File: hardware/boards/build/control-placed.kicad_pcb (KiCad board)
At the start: 4 copper layers, 177.9 x 107.5 mm, 132 parts

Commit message: Fix firmware
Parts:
- removed the REF** at (69.8, 51.4)
- removed the REF** at (69.8, 36.2)
- removed the REF** at (39.4, 59.0)
- removed the REF** at (77.4, 21.0)
- removed the REF** at (54.6, 43.8)
- removed the REF** at (69.8, 21.0)
- removed the REF** at (25.9, 71.9)
- removed the REF** at (54.6, 36.2)
- removed the REF** at (54.6, 59.0)
- added REF**: R_Array_Convex_4x0603, ResArray4x0603:R_Array_Convex_4x0603, B.Cu at (31.8, 59.0)
- added REF**: SOIC-16, 74HC165D:SOIC-16, B.Cu at (77.4, 51.4)
- added REF**: SOIC-16, 74HC165D:SOIC-16, B.Cu at (62.2, 59.0)
- added REF**: R_Array_Convex_4x0603, ResArray4x0603:R_Array_Convex_4x0603, B.Cu at (77.4, 36.2)
- added REF**: R_Array_Convex_4x0603, ResArray4x0603:R_Array_Convex_4x0603, B.Cu at (77.4, 28.6)
- added REF**: SOIC-16, 74HC165D:SOIC-16, B.Cu at (47.0, 59.0)
- added REF**: R_Array_Convex_4x0603, ResArray4x0603:R_Array_Convex_4x0603, B.Cu at (69.8, 28.6)
- added REF**: SOIC-16, 74HC165D:SOIC-16, B.Cu at (62.2, 43.8)
- added REF**: R_Array_Convex_4x0603, ResArray4x0603:R_Array_Convex_4x0603, B.Cu at (62.2, 28.6)
- moved C10 92.3 mm to (85.0, 5.80)
- moved C18 87.1 mm to (115.2, 63.9)
- moved C15 85.2 mm to (85.0, 21.0)
- moved R16 83.9 mm to (39.4, 28.6)
- moved C16 80.6 mm to (47.0, 21.0)
- moved C8 75.8 mm to (107.9, 95.2)
- moved C20 53.7 mm to (39.4, 43.8)
- moved C4 53.7 mm to (31.8, 43.8)
- moved C21 51.0 mm to (77.4, 5.80)
- moved C22 51.0 mm to (77.4, 13.4)
- moved C5 34.0 mm to (31.8, 51.4)
- moved C17 34.0 mm to (69.8, 13.4)
- moved C12 32.3 mm to (122.6, 17.7)
- moved C25 31.3 mm to (115.7, 71.7)
- moved R1 31.2 mm to (25.9, 71.9)
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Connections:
- REF** pad 1: buttons-1-3 -> buttons-1-4
- REF** pad 2: buttons-R2A-3 -> buttons-R2A-5
- REF** pad 3: buttons-R3A-3 -> buttons-R3A-5
- REF** pad 4: buttons-R4A-4 -> buttons-R4A-6
- REF** pad 10: QH -> lv
- REF** pad 11: buttons-1-5 -> buttons-1-2
- REF** pad 12: buttons-R2A-2 -> buttons-R2A-4
- REF** pad 13: buttons-R3A-2 -> buttons-R3A-4
- REF** pad 14: buttons-R4A-3 -> buttons-R4A-5
- REF** pad 3: buttons-1-3 -> buttons-1-4
- REF** pad 4: buttons-R2A-3 -> buttons-R2A-5
- REF** pad 5: buttons-R3A-3 -> buttons-R3A-5
- REF** pad 6: buttons-R4A-4 -> buttons-R4A-6
- REF** pad 7: buttons.sr2-QH_N -> QH_N
- REF** pad 9: buttons-QH -> QH
- REF** pad 1: buttons-1 -> buttons-1-7
- REF** pad 2: buttons-R2A -> buttons-R2A-7
- REF** pad 3: buttons-R3A-1 -> R3A
- REF** pad 4: buttons-R4A -> buttons-R4A-2
- REF** pad 1: buttons-1-2 -> buttons-1-6
- REF** pad 2: buttons-R2A-4 -> buttons-R2A-6
- REF** pad 3: buttons-R3A-4 -> buttons-R3A-6
- REF** pad 4: buttons-R4A-5 -> buttons-R4A-7
- REF** pad 1: buttons-1-4 -> buttons-1-3
- REF** pad 2: buttons-R2A-5 -> buttons-R2A-3
- REF** pad 3: buttons-R3A-5 -> buttons-R3A-3
- REF** pad 4: buttons-R4A-6 -> buttons-R4A-4

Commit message: Fix visuals
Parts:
- removed the REF** at (107.9, 63.9)
- removed the REF** at (85.0, 36.2)
- added REF**: R_Array_Convex_4x0603, ResArray4x0603:R_Array_Convex_4x0603, B.Cu at (92.6, 59.0)
- added REF**: R_Array_Convex_4x0603, ResArray4x0603:R_Array_Convex_4x0603, B.Cu at (92.6, 51.4)
- moved C9 124.6 mm to (21.4, 13.4)
- moved C18 116.9 mm to (13.8, 5.79)
- moved R7 98.7 mm to (158.0, 6.00)
- moved C25 89.9 mm to (54.6, 5.80)
- moved R6 88.5 mm to (150.0, 6.00)
- moved C14 87.7 mm to (6.47, 52.5)
- moved C23 81.6 mm to (6.47, 61.4)
- moved R9 81.1 mm to (31.8, 43.8)
- moved R8 72.5 mm to (122.6, 8.58)
- moved C13 64.9 mm to (31.8, 36.2)
- moved REF** 62.3 mm to (122.6, 17.7)
- moved R16 54.0 mm to (88.4, 51.2)
- moved C10 53.7 mm to (31.8, 13.4)
- moved C7 53.7 mm to (39.4, 13.4)
- moved C6 53.2 mm to (39.4, 21.0)
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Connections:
- REF** pad 1: buttons-1 -> buttons-1-7
- REF** pad 2: buttons-R2A -> buttons-R2A-7
- REF** pad 3: buttons-R3A-1 -> R3A
- REF** pad 4: buttons-R4A -> buttons-R4A-2
- REF** pad 7: QH_N -> (no net)
- REF** pad 7: buttons.sr5-QH_N -> (no net)
- REF** pad 3: NC -> (no net)
- REF** pad 1: buttons-1-5 -> buttons-1-1
- REF** pad 2: buttons-R2A-2 -> R2A
- REF** pad 3: buttons-R3A-2 -> buttons-R3A
- REF** pad 4: buttons-R4A-3 -> R4A
- REF** pad 7: buttons.sr4-QH_N -> (no net)
- REF** pad 7: buttons.sr2-QH_N -> (no net)
- REF** pad 1: buttons-1-3 -> buttons-1-4
- REF** pad 2: buttons-R2A-3 -> buttons-R2A-5
- REF** pad 3: buttons-R3A-3 -> buttons-R3A-5
- REF** pad 4: buttons-R4A-4 -> buttons-R4A-6
- REF** pad 1: buttons-1-2 -> buttons-1-5
- REF** pad 2: buttons-R2A-4 -> buttons-R2A-2
- REF** pad 3: buttons-R3A-4 -> buttons-R3A-2
- REF** pad 4: buttons-R4A-5 -> buttons-R4A-3
- REF** pad 1: buttons-1-1 -> buttons-1-3
- REF** pad 2: R2A -> buttons-R2A-3
- REF** pad 3: buttons-R3A -> buttons-R3A-3
- REF** pad 4: R4A -> buttons-R4A-4
- REF** pad 7: buttons.sr3-QH_N -> (no net)
- U6 pad 21: INTB -> (no net)
- U7 pad 21: leds.led_b-INTB -> (no net)
- U8 pad 21: leds.led_c-INTB -> (no net)

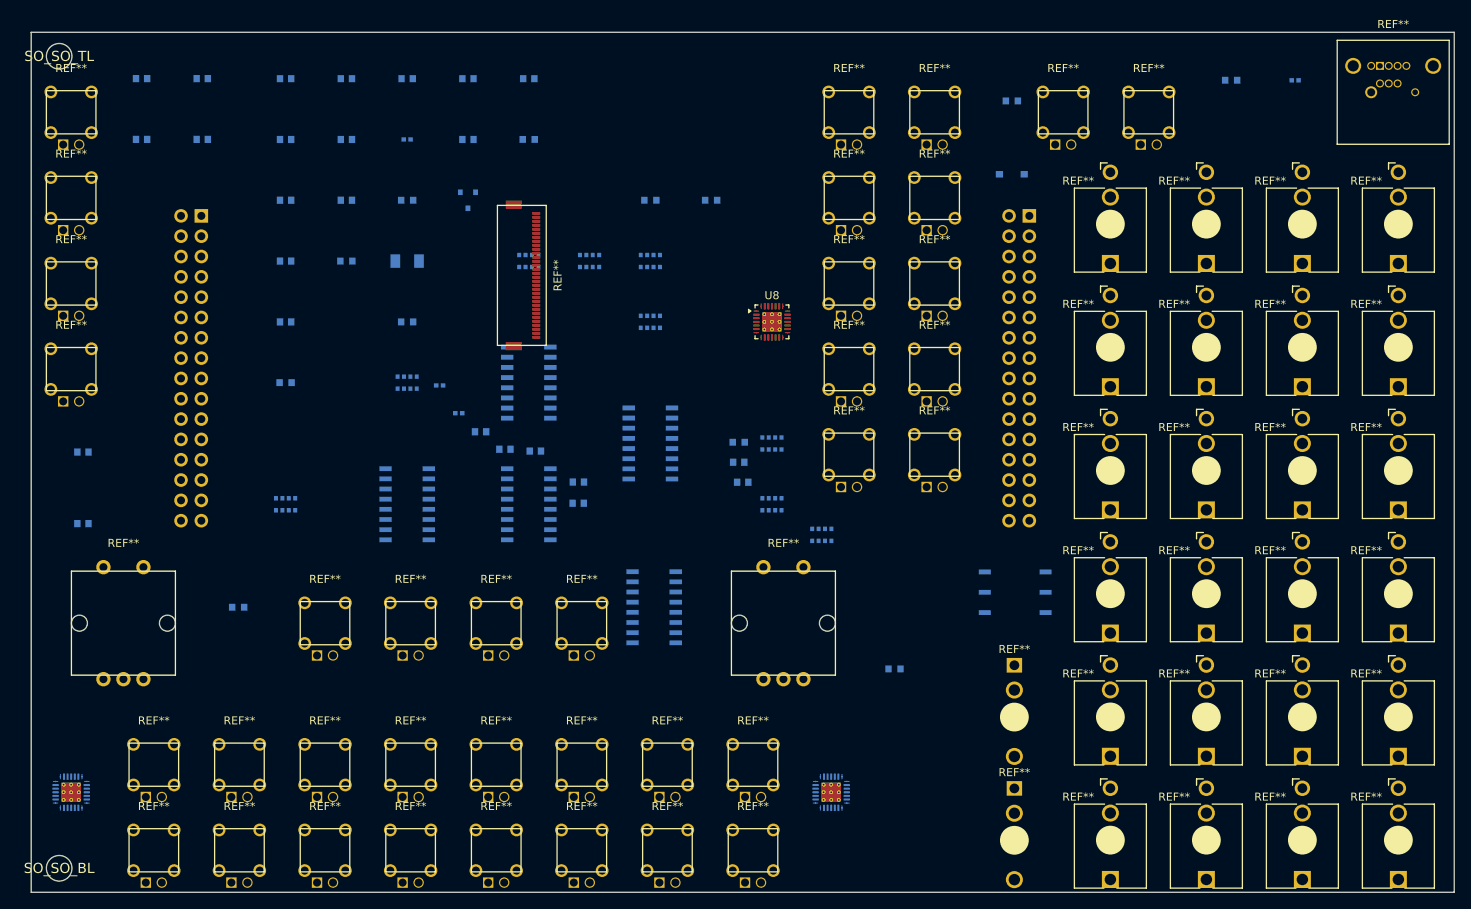
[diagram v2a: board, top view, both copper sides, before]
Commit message: production check command and fixes coming out of that
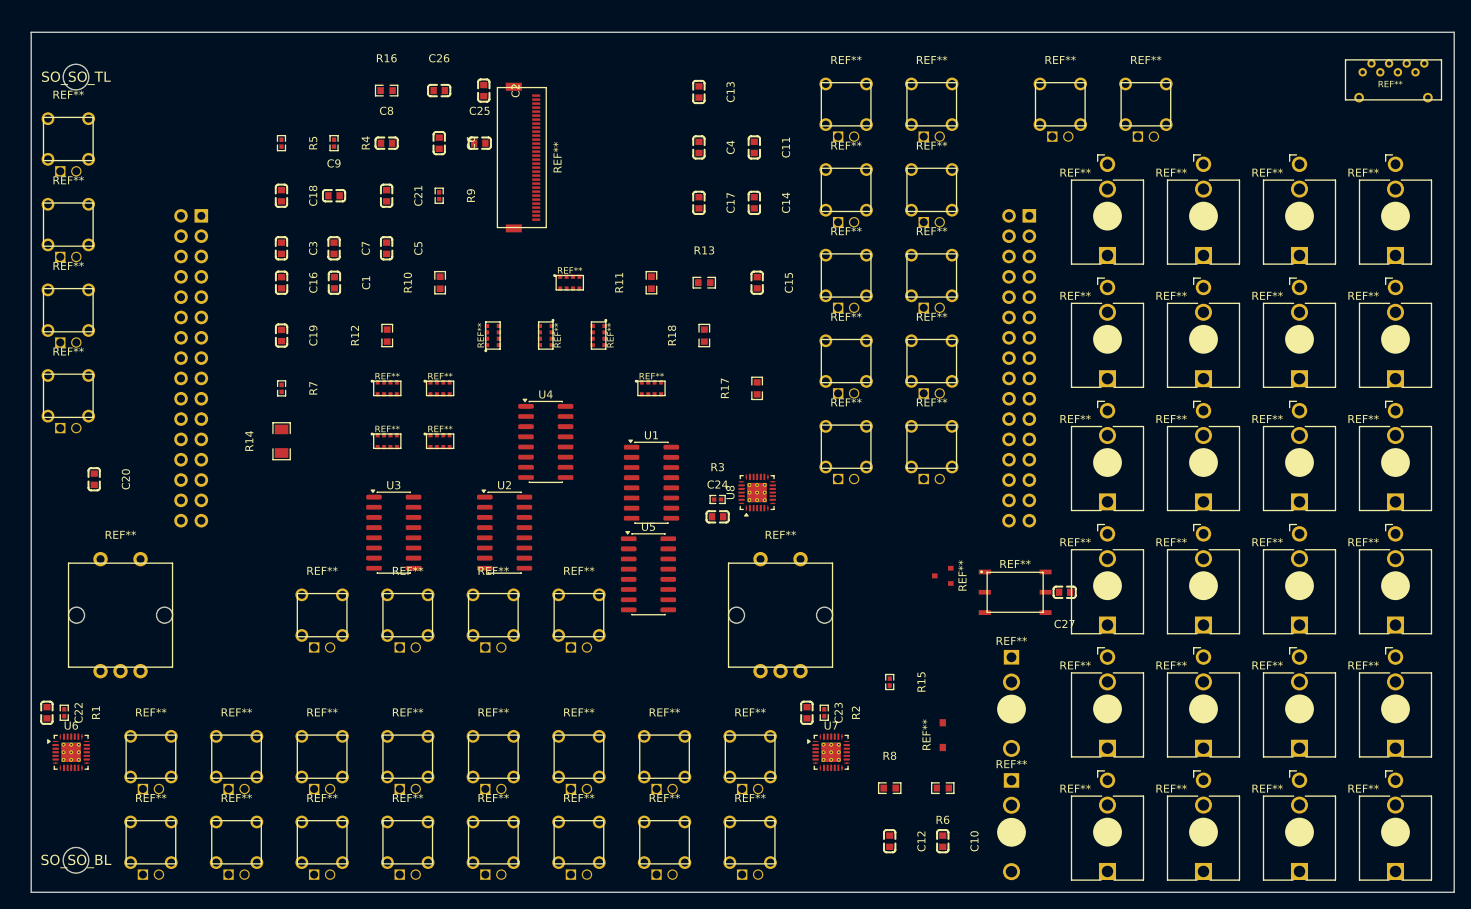
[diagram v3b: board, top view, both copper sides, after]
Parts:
- removed the REF** at (68.8, 102.2)
- removed the REF** at (134.9, 79.1)
- removed the REF** at (94.0, 73.9)
- removed the REF** at (79.5, 91.5)
- removed the REF** at (134.9, 17.5)
- removed the REF** at (58.1, 73.9)
- removed the REF** at (146.9, 48.3)
- removed the REF** at (5.00, 42.1)
- removed the REF** at (112.9, 10.0)
- removed the REF** at (112.9, 31.4)
- removed the REF** at (122.9, 101.0)
- removed the REF** at (146.9, 79.1)
- removed the REF** at (36.7, 73.9)
- removed the REF** at (146.9, 32.9)
- removed the REF** at (134.9, 63.7)
- removed the REF** at (134.9, 48.3)
- removed the REF** at (36.7, 102.2)
- removed the REF** at (146.9, 94.5)
- removed the REF** at (170.9, 94.5)
- removed the REF** at (112.9, 52.8)
- removed the REF** at (5.00, 10.0)
- removed the REF** at (102.2, 52.8)
- removed the REF** at (47.4, 91.5)
- removed the REF** at (134.9, 94.5)
- removed the REF** at (170.9, 48.3)
- removed the REF** at (79.5, 102.2)
- removed the REF** at (68.8, 73.9)
- removed the REF** at (122.9, 85.6)
- removed the REF** at (15.3, 102.2)
- removed the REF** at (158.9, 79.1)
- removed the REF** at (129.0, 10.0)
- removed the REF** at (170.9, 17.5)
- removed the REF** at (90.2, 102.2)
- removed the REF** at (102.2, 20.7)
- removed the REF** at (112.9, 42.1)
- removed the REF** at (58.1, 102.2)
- removed the REF** at (11.5, 73.9)
- removed the REF** at (158.9, 63.7)
- removed the REF** at (5.00, 31.4)
- removed the REF** at (146.9, 17.5)
- removed the REF** at (26.0, 102.2)
- removed the REF** at (112.9, 20.7)
- removed the REF** at (170.9, 79.1)
- removed the REF** at (158.9, 94.5)
- removed the REF** at (90.2, 91.5)
- removed the REF** at (5.00, 20.7)
- removed the REF** at (158.9, 32.9)
- removed the REF** at (58.1, 91.5)
- removed the REF** at (170.9, 32.9)
- removed the REF** at (146.9, 63.7)
- removed the REF** at (134.9, 32.9)
- removed the REF** at (68.8, 91.5)
- removed the REF** at (170.9, 63.7)
- removed the REF** at (26.0, 91.5)
- removed the REF** at (139.7, 10.0)
- removed the REF** at (102.2, 10.0)
- removed the REF** at (158.9, 17.5)
- removed the REF** at (102.2, 42.1)
- removed the REF** at (47.4, 102.2)
- removed the REF** at (36.7, 91.5)
- removed the REF** at (102.2, 31.4)
- removed the REF** at (77.4, 28.6)
- removed the REF** at (77.9, 71.9)
- removed the REF** at (62.2, 43.8)
- removed the REF** at (47.4, 73.9)
- removed the REF** at (77.4, 36.2)
- removed the REF** at (62.2, 28.6)
- removed the REF** at (77.4, 51.4)
- removed the REF** at (47.0, 43.8)
- removed the REF** at (62.2, 59.0)
- removed the REF** at (92.6, 59.0)
- removed the REF** at (158.9, 48.3)
- removed the REF** at (98.8, 62.8)
- removed the REF** at (31.8, 59.0)
- removed the REF** at (69.8, 28.6)
- removed the REF** at (92.6, 51.4)
- removed the REF** at (47.0, 59.0)
- removed the REF** at (15.3, 91.5)
- added C26: 100nF, YAGEO_CC0603KRX7R9BB104:C0603, F.Cu at (51.0, 7.29)
- added C27: 100nF, YAGEO_CC0603KRX7R9BB104:C0603, F.Cu at (129.2, 70.0)
- added R18: 47kΩ, UNI_ROYAL_0603WAF4702T5E:R0603, F.Cu at (84.1, 37.9)
- added REF**: PB6149L, PB6149L:PB6149L, F.Cu at (112.6, 30.4)
- added REF**: WQP518MA, WQP518MA:WQP518MA, F.Cu at (146.5, 16.5)
- added REF**: R_Array_Convex_4x0603, ResArray4x0603:R_Array_Convex_4x0603, F.Cu at (44.5, 51.1)
- added REF**: PB6149L, PB6149L:PB6149L, F.Cu at (15.0, 90.5)
- added REF**: PB6149L, PB6149L:PB6149L, F.Cu at (47.1, 90.5)
- added REF**: PB6149L, PB6149L:PB6149L, F.Cu at (36.4, 101.2)
- added REF**: PB6149L, PB6149L:PB6149L, F.Cu at (68.5, 90.5)
- added REF**: EC11E, EC11E:EC11E, F.Cu at (93.7, 72.9)
- added REF**: PB6149L, PB6149L:PB6149L, F.Cu at (36.4, 90.5)
- added REF**: PB6149L, PB6149L:PB6149L, F.Cu at (128.6, 9.00)
- added REF**: PB6149L, PB6149L:PB6149L, F.Cu at (112.6, 19.7)
- added REF**: WQP518MA, WQP518MA:WQP518MA, F.Cu at (134.5, 78.1)
- added REF**: PB6149L, PB6149L:PB6149L, F.Cu at (112.6, 9.00)
- added REF**: PB6149L, PB6149L:PB6149L, F.Cu at (101.9, 41.1)
- added REF**: WQP518MA, WQP518MA:WQP518MA, F.Cu at (170.5, 31.9)
- added REF**: PB6149L, PB6149L:PB6149L, F.Cu at (139.3, 9.00)
- added REF**: R_Array_Convex_4x0603, ResArray4x0603:R_Array_Convex_4x0603, F.Cu at (67.3, 31.3)
- added REF**: WQP518MA, WQP518MA:WQP518MA, F.Cu at (170.5, 62.7)
- added REF**: WQP518MA, WQP518MA:WQP518MA, F.Cu at (158.5, 16.5)
- added REF**: PB6149L, PB6149L:PB6149L, F.Cu at (57.8, 101.2)
- added REF**: WQP518MA, WQP518MA:WQP518MA, F.Cu at (170.5, 16.5)
- added REF**: WQP518MA, WQP518MA:WQP518MA, F.Cu at (158.5, 62.7)
- added REF**: PJ366ST, PJ366ST:PJ366ST, F.Cu at (122.5, 100.0)
- added REF**: PJ366ST, PJ366ST:PJ366ST, F.Cu at (122.5, 84.6)
- added REF**: WQP518MA, WQP518MA:WQP518MA, F.Cu at (134.5, 31.9)
- added REF**: PB6149L, PB6149L:PB6149L, F.Cu at (79.2, 101.2)
- added REF**: WQP518MA, WQP518MA:WQP518MA, F.Cu at (146.5, 93.5)
- added REF**: EC11E, EC11E:EC11E, F.Cu at (11.2, 72.9)
- added REF**: R_Array_Convex_4x0603, ResArray4x0603:R_Array_Convex_4x0603, F.Cu at (44.5, 44.5)
- added REF**: R_Array_Convex_4x0603, ResArray4x0603:R_Array_Convex_4x0603, F.Cu at (70.9, 37.9)
- added REF**: PB6149L, PB6149L:PB6149L, F.Cu at (25.7, 101.2)
- added REF**: WQP518MA, WQP518MA:WQP518MA, F.Cu at (134.5, 62.7)
- added REF**: WQP518MA, WQP518MA:WQP518MA, F.Cu at (134.5, 93.5)
- added REF**: R_Array_Convex_4x0603, ResArray4x0603:R_Array_Convex_4x0603, F.Cu at (51.1, 51.1)
- added REF**: WQP518MA, WQP518MA:WQP518MA, F.Cu at (146.5, 47.3)
- added REF**: PB6149L, PB6149L:PB6149L, F.Cu at (4.64, 24.0)
- added REF**: WQP518MA, WQP518MA:WQP518MA, F.Cu at (134.5, 16.5)
- added REF**: PB6149L, PB6149L:PB6149L, F.Cu at (47.1, 72.9)
- added REF**: PB6149L, PB6149L:PB6149L, F.Cu at (112.6, 51.8)
- added REF**: PB6149L, PB6149L:PB6149L, F.Cu at (4.64, 13.3)
- added REF**: WQP518MA, WQP518MA:WQP518MA, F.Cu at (134.5, 47.3)
- added REF**: WQP518MA, WQP518MA:WQP518MA, F.Cu at (146.5, 78.1)
- added REF**: PB6149L, PB6149L:PB6149L, F.Cu at (15.0, 101.2)
- added REF**: WQP518MA, WQP518MA:WQP518MA, F.Cu at (146.5, 62.7)
- added REF**: WQP518MA, WQP518MA:WQP518MA, F.Cu at (170.5, 47.3)
- added REF**: PB6149L, PB6149L:PB6149L, F.Cu at (79.2, 90.5)
- added REF**: WQP518MA, WQP518MA:WQP518MA, F.Cu at (158.5, 31.9)
- added REF**: PB6149L, PB6149L:PB6149L, F.Cu at (112.6, 41.1)
- added REF**: R_Array_Convex_4x0603, ResArray4x0603:R_Array_Convex_4x0603, F.Cu at (57.7, 37.9)
- added REF**: R_Array_Convex_4x0603, ResArray4x0603:R_Array_Convex_4x0603, F.Cu at (77.5, 44.5)
- added REF**: PB6149L, PB6149L:PB6149L, F.Cu at (89.9, 90.5)
- added REF**: PB6149L, PB6149L:PB6149L, F.Cu at (89.9, 101.2)
- added REF**: R_Array_Convex_4x0603, ResArray4x0603:R_Array_Convex_4x0603, F.Cu at (64.3, 37.9)
- added REF**: WQP518MA, WQP518MA:WQP518MA, F.Cu at (146.5, 31.9)
- added REF**: WQP518MA, WQP518MA:WQP518MA, F.Cu at (158.5, 47.3)
- added REF**: PB6149L, PB6149L:PB6149L, F.Cu at (101.9, 9.00)
- added REF**: PB6149L, PB6149L:PB6149L, F.Cu at (4.64, 45.4)
- added REF**: WQP518MA, WQP518MA:WQP518MA, F.Cu at (158.5, 93.5)
- added REF**: WQP518MA, WQP518MA:WQP518MA, F.Cu at (158.5, 78.1)
- added REF**: PB6149L, PB6149L:PB6149L, F.Cu at (57.8, 72.9)
- added REF**: PB6149L, PB6149L:PB6149L, F.Cu at (47.1, 101.2)
- added REF**: WQP518MA, WQP518MA:WQP518MA, F.Cu at (170.5, 93.5)
- added REF**: PB6149L, PB6149L:PB6149L, F.Cu at (57.8, 90.5)
- added REF**: PB6149L, PB6149L:PB6149L, F.Cu at (25.7, 90.5)
- added REF**: PB6149L, PB6149L:PB6149L, F.Cu at (101.9, 19.7)
- added REF**: PB6149L, PB6149L:PB6149L, F.Cu at (36.4, 72.9)
- added REF**: WQP518MA, WQP518MA:WQP518MA, F.Cu at (170.5, 78.1)
- added REF**: PB6149L, PB6149L:PB6149L, F.Cu at (68.5, 72.9)
- added REF**: PB6149L, PB6149L:PB6149L, F.Cu at (4.64, 34.7)
- added REF**: PB6149L, PB6149L:PB6149L, F.Cu at (68.5, 101.2)
- added REF**: R_Array_Convex_4x0603, ResArray4x0603:R_Array_Convex_4x0603, F.Cu at (51.1, 44.5)
- added REF**: PB6149L, PB6149L:PB6149L, F.Cu at (101.9, 30.4)
- added REF**: PB6149L, PB6149L:PB6149L, F.Cu at (101.9, 51.8)
- added U1: , 74HC165D:SOIC-16, F.Cu at (77.5, 56.3)
- added U2: , 74HC165D:SOIC-16, F.Cu at (59.2, 62.6)
- added U3: , 74HC165D:SOIC-16, F.Cu at (45.3, 62.6)
- added U4: , 74HC165D:SOIC-16, F.Cu at (64.3, 51.2)
- added U5: , 74HC165D:SOIC-16, F.Cu at (77.2, 67.7)
- C1, C10, C11, C12, C13, C14, C15, C16, C17, C18, C2, C20, C22, C24, C3, C4, C5, C6, C7, C9, R10, R11, R12, R13, R14, R15, R16, R4, R5, R6, R7, R8, REF** (x3), U6, U7: moved to F.Cu
- C19, C23: value 10µF -> 100nF; footprint Samsung_Electro_Mechanics_CL10A106KP8NNNC:C0603 -> YAGEO_CC0603KRX7R9BB104:C0603; moved to F.Cu
- C21, C25, C8: value 100nF -> 10µF; footprint YAGEO_CC0603KRX7R9BB104:C0603 -> Samsung_Electro_Mechanics_CL10A106KP8NNNC:C0603; moved to F.Cu
- R1, R2, R3: value 3.3kΩ -> 100kΩ; footprint UNI_ROYAL_0603WAF3301T5E:R0603 -> UNI_ROYAL_0402WGF1003TCE:R0402; moved to F.Cu
- R17: value 47kΩ -> 10kΩ; footprint UNI_ROYAL_0603WAF4702T5E:R0603 -> UNI_ROYAL_0603WAF1002T5E:R0603; moved to F.Cu
- R9: value 1kΩ -> 4.7kΩ; footprint UNI_ROYAL_0603WAF1001T5E:R0603 -> UNI_ROYAL_0402WGF4701TCE:R0402; moved to F.Cu
- REF**: value PJS008U -> PJS008U-3000-0
- moved R7 132.4 mm to (31.3, 44.5), turned to -90 degrees
- moved C10 120.2 mm to (113.9, 101.1), turned to -90 degrees
- moved R6 95.5 mm to (113.9, 94.5)
- moved C23 93.5 mm to (97.0, 85.1), turned to -90 degrees
- moved R15 90.8 mm to (107.3, 81.2), turned to -90 degrees
- moved C14 89.5 mm to (90.4, 21.3), turned to -90 degrees
- moved C22 87.7 mm to (1.96, 85.1), turned to -90 degrees
- moved R8 87.2 mm to (107.3, 94.5), turned to 0 degrees
- moved REF** 75.7 mm to (113.9, 67.9), turned to -90 degrees
- moved REF** 70.6 mm to (113.9, 87.8), turned to 90 degrees
- moved C4 69.7 mm to (83.5, 14.4), turned to -90 degrees
- moved R16 62.2 mm to (44.4, 7.29), turned to 0 degrees
- moved C8 59.4 mm to (44.4, 13.9), turned to 0 degrees
- moved C13 59.1 mm to (83.5, 7.46), turned to -90 degrees
- moved C2 50.3 mm to (56.6, 7.29), turned to -90 degrees
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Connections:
- C10 pad 1: c_cv_c-power-hv -> c_cv_a-power-hv
- C11 pad 1: c_cv_d-power-hv -> c_cv_b-power-hv
- C12 pad 1: c_lcd_rst-power-hv -> c_cv_c-power-hv
- C13 pad 1: c_sd-power-hv -> c_cv_d-power-hv
- C14 pad 1: c_sd-power-hv -> c_lcd_rst-power-hv
- C20 pad 1: c_filt_a-power-hv -> c_sd-power-hv
- C21 pad 1: c_filt_b-power-hv -> c_sd-power-hv
- C22 pad 1: c_filt_c-power-hv -> c_filt_a-power-hv
- C23 pad 1: hv -> c_filt_b-power-hv
- C24 pad 1: hv -> c_filt_c-power-hv
- C25 pad 1: c_sd-power-hv -> hv
- C6 pad 1: hv -> c_sd-power-hv
- C7 pad 1: hv -> c_sd-power-hv
- C8 pad 1: c_cv_a-power-hv -> hv
- C9 pad 1: c_cv_b-power-hv -> hv
- R17 pad 2: miso -> cs
- R6 pad 2: CATHODE -> 2
- REF** pad 1: CATHODE -> midi-1
- REF** pad 9: cd -> lv
- REF** pad 1: 2 -> midi-1
- REF** pad 2: CATHODE -> 2
- REF** pad 4: lv -> midi_rx
- REF** pad 5: midi_rx -> lv
- REF** pad 6: c_sd-power-hv -> hv
- REF** pad 10: sck -> mosi
- REF** pad 11: miso -> lcd_cs
- REF** pad 12: lcd_cs -> miso
- REF** pad 13: lcd_dc -> lcd_bl
- REF** pad 14: lcd_bl -> lcd_dc
- REF** pad 15: cs -> sd_cd
- REF** pad 16: cd -> cs
- REF** pad 17: midi_tx -> midi_rx
- REF** pad 18: midi_rx -> midi_tx
- REF** pad 19: A-1 -> B-1
- REF** pad 20: B-1 -> A-1
- REF** pad 21: enc_b_sw -> CLK
- REF** pad 22: CLK -> enc_b_sw
- REF** pad 23: SH_LD -> data_out
- REF** pad 24: data_out -> SH_LD
- REF** pad 25: SDA -> SCL
- REF** pad 26: SCL -> SDA
- REF** pad 29: A -> B
- REF** pad 30: B -> A
- REF** pad 31: enc_a_sw -> lv
- REF** pad 32: lv -> enc_a_sw
- REF** pad 7: v12p -> v12n
- REF** pad 8: v12n -> v12p
- REF** pad 9: mosi -> sck
- REF** pad 10: c_cv_c-power-hv -> c_cv_b-power-hv
- REF** pad 11: c_cv_d-power-hv -> lv
- REF** pad 12: lv -> c_cv_d-power-hv
- REF** pad 13: gate1 -> gate2
- REF** pad 14: gate2 -> gate1
- REF** pad 15: gate3 -> gate4
- REF** pad 16: gate4 -> gate3
- REF** pad 17: lv -> pitch1
- REF** pad 18: pitch1 -> lv
- REF** pad 19: pitch2 -> pitch3
- REF** pad 20: pitch3 -> pitch2
- REF** pad 21: pitch4 -> lv
- REF** pad 22: lv -> pitch4
- REF** pad 23: vel1 -> vel2
- REF** pad 24: vel2 -> vel1
- REF** pad 25: vel3 -> vel4
- REF** pad 26: vel4 -> vel3
- REF** pad 27: lv -> mod1
- REF** pad 28: mod1 -> lv
- REF** pad 29: mod2 -> mod3
- REF** pad 3: clk_in -> clk_out
- REF** pad 30: mod3 -> mod2
- REF** pad 31: mod4 -> lv
- REF** pad 32: lv -> mod4
- REF** pad 4: clk_out -> clk_in
- REF** pad 5: rst_in -> rst_out
- REF** pad 6: rst_out -> rst_in
- REF** pad 7: c_lcd_rst-power-hv -> c_cv_a-power-hv
- REF** pad 8: c_cv_a-power-hv -> c_lcd_rst-power-hv
- REF** pad 9: c_cv_b-power-hv -> c_cv_c-power-hv

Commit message: Increase cutouts for encoders & jacks
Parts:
- removed the REF** at (44.5, 51.1)
- removed the REF** at (44.5, 44.5)
- added REF**: R_Array_Convex_4x0603, ResArray4x0603:R_Array_Convex_4x0603, F.Cu at (77.5, 37.9)
- added REF**: R_Array_Convex_4x0603, ResArray4x0603:R_Array_Convex_4x0603, F.Cu at (71.4, 31.3)
- moved C10 113.0 mm to (51.0, 7.29), turned to 180 degrees
- moved C12 106.5 mm to (37.9, 20.4), turned to 180 degrees
- moved C21 97.1 mm to (107.3, 94.5)
- moved C8 97.1 mm to (107.3, 87.8)
- moved C16 95.6 mm to (116.9, 74.0)
- moved C25 93.9 mm to (113.9, 87.8), turned to -90 degrees
- moved C5 88.2 mm to (113.9, 81.2)
- moved C4 84.7 mm to (102.8, 96.8)
- moved R15 83.0 mm to (44.4, 27.0)
- moved REF** 81.8 mm to (37.9, 37.9), turned to 180 degrees
- moved C14 81.6 mm to (107.3, 101.1), turned to 180 degrees
- moved C13 67.3 mm to (112.9, 67.9), turned to 180 degrees
- moved R7 60.2 mm to (83.5, 14.4)
- moved R5 59.1 mm to (90.4, 14.4)
- moved C24 53.2 mm to (33.0, 54.0)
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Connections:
- REF** pad 1: buttons-1 -> buttons-1-1
- REF** pad 2: buttons-R2A -> R2A
- REF** pad 3: buttons-R3A-1 -> buttons-R3A
- REF** pad 4: buttons-R4A -> R4A
- REF** pad 1: buttons-1-7 -> 1
- REF** pad 2: buttons-R2A-7 -> buttons-R2A-1
- REF** pad 3: R3A -> buttons-R3A-7
- REF** pad 4: buttons-R4A-2 -> buttons-R4A-1
- REF** pad 1: buttons-1-2 -> buttons-1-6
- REF** pad 2: buttons-R2A-4 -> buttons-R2A-6
- REF** pad 3: buttons-R3A-4 -> buttons-R3A-6
- REF** pad 4: buttons-R4A-5 -> buttons-R4A-7
- REF** pad 1: 1 -> buttons-1-3
- REF** pad 2: buttons-R2A-1 -> buttons-R2A-3
- REF** pad 3: buttons-R3A-7 -> buttons-R3A-3
- REF** pad 4: buttons-R4A-1 -> buttons-R4A-4
- REF** pad 1: buttons-1-3 -> buttons-1
- REF** pad 2: buttons-R2A-3 -> buttons-R2A
- REF** pad 3: buttons-R3A-3 -> buttons-R3A-1
- REF** pad 4: buttons-R4A-4 -> buttons-R4A
- REF** pad 1: buttons-1-6 -> buttons-1-5
- REF** pad 2: buttons-R2A-6 -> buttons-R2A-2
- REF** pad 3: buttons-R3A-6 -> buttons-R3A-2
- REF** pad 4: buttons-R4A-7 -> buttons-R4A-3
- REF** pad 1: buttons-1-5 -> buttons-1-2
- REF** pad 2: buttons-R2A-2 -> buttons-R2A-4
- REF** pad 3: buttons-R3A-2 -> buttons-R3A-4
- REF** pad 4: buttons-R4A-3 -> buttons-R4A-5
